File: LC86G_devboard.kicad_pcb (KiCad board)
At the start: 4 copper layers, 40 x 40 mm, 15 parts, among them J1 Conn_01x09_Pin, J2 U.FL-R-SMT_10_, Q1 DTC143Z, Q2 DTC143Z, Q3 AO3415, U1 LC86G

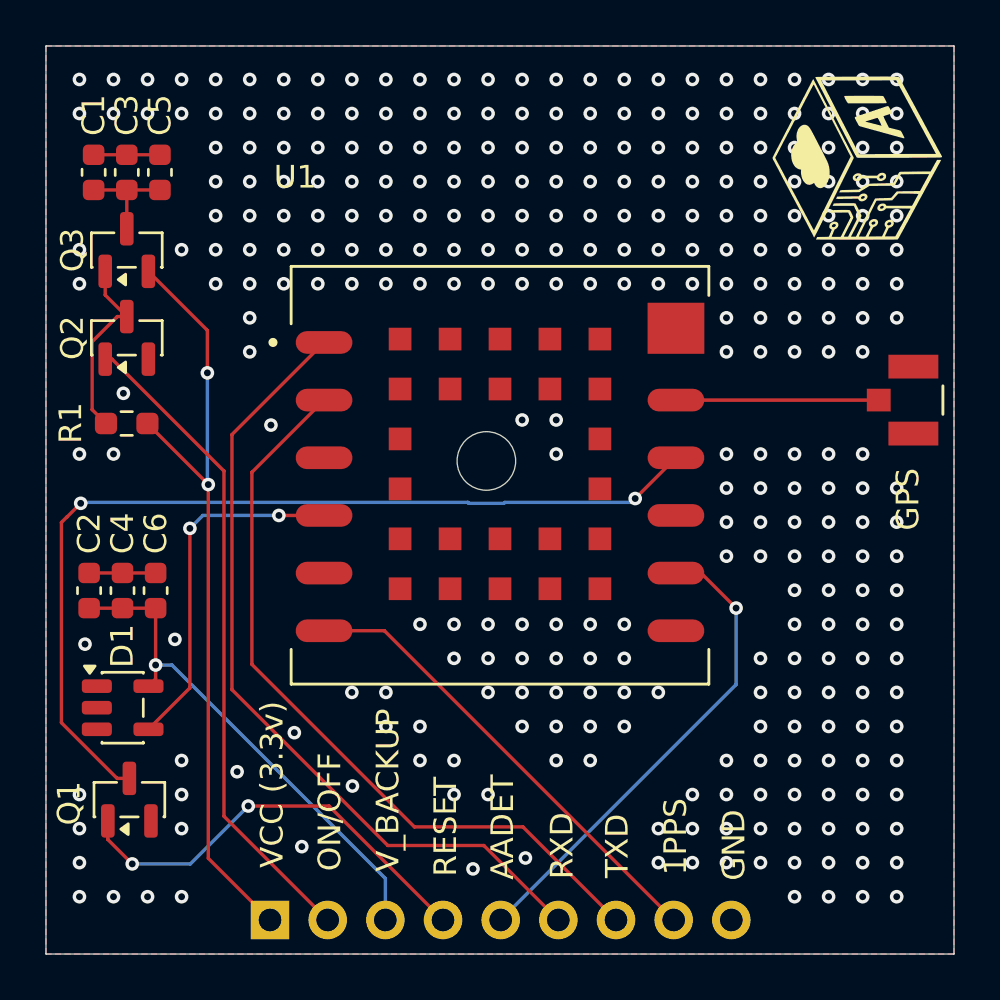
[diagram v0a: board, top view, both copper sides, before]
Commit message: pistas faltantes ruteadas
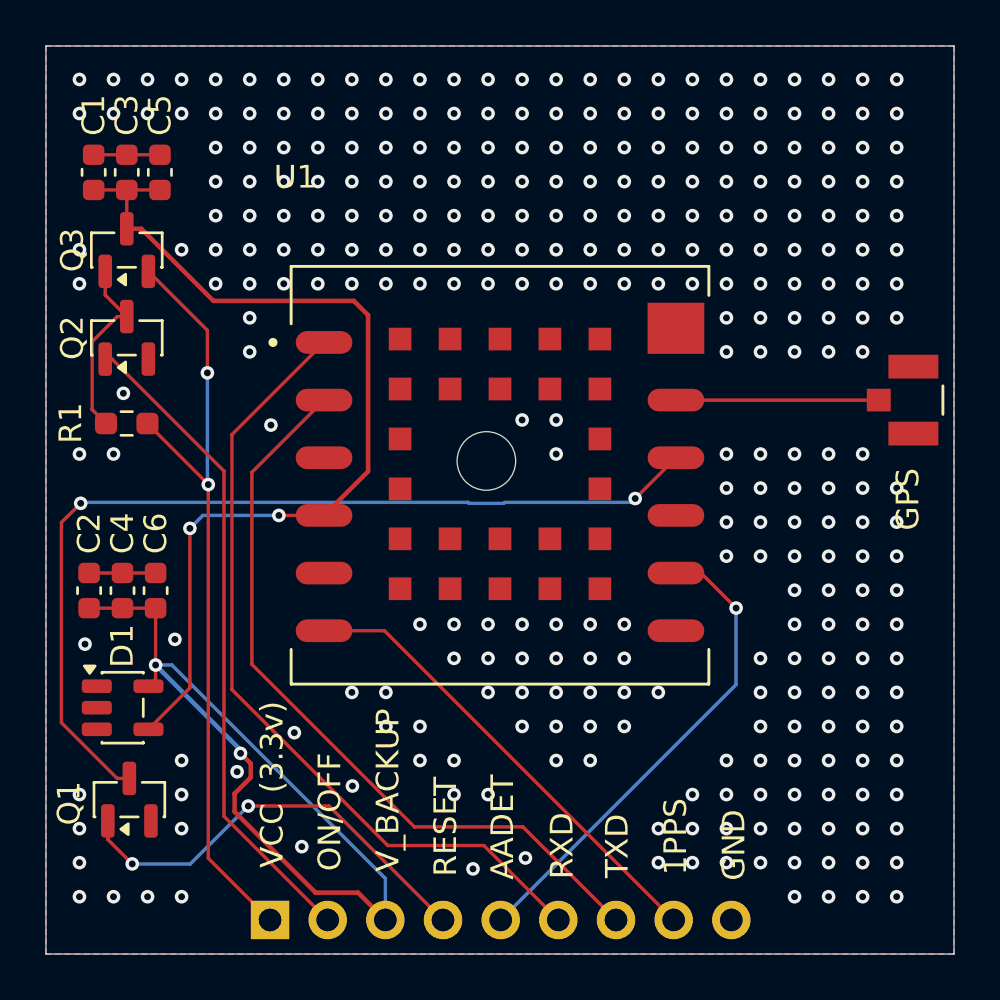
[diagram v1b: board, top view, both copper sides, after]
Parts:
- removed G***: LOGO, Images:LOGOv3.2
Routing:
- net /LC86G.VCC: track 20.5 -> 42.3 mm
- net /V_BCKP: track 22.4 -> 39.5 mm, vias 1 -> 2

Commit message: carga final
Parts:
- removed J1: Conn_01x09_Pin, Connector_PinHeader_2.54mm:PinHeader_1x09_P2.54mm_Vertical
- added D2: LED_Small, LED_SMD:LED_0603_1608Metric, F.Cu at (146.4, 106.2)
- added J3: Conn_01x10_Pin, Connector_PinHeader_2.54mm:PinHeader_1x10_P2.54mm_Vertical, B.Cu at (151.5, 109.1)
- added Power indicator: SolderJumper_2_Open, Jumper:SolderJumper-2_P1.3mm_Open_TrianglePad1.0x1.5mm, B.Cu at (145.2, 108.8)
- added R2: 4.7k, Resistor_SMD:R_0603_1608Metric_Pad0.98x0.95mm_HandSolder, F.Cu at (146.4, 108.6)
- added U2: XC6206P332MR, EasyEDA:SOT-23-3_L2.9-W1.6-P1.90-LS2.8-BR, F.Cu at (146.7, 102.9)
- added kibuzzard-6A1C8FBC: G***, kibuzzard-6A1C8FBC, F.Cu at (166.0, 73.1)
- moved Q1 4.67 mm to (146.7, 99.0), turned to 180 degrees
- moved D1 4.52 mm to (146.8, 95.2)
- moved C6 3.79 mm to (148.6, 90.8)
- moved C4 3.75 mm to (146.8, 90.8)
- moved C2 3.73 mm to (145.0, 90.8)
- moved C5 1.43 mm to (148.6, 74.7)
- moved C3 1.36 mm to (146.8, 74.7)
- moved C1 1.35 mm to (145.0, 74.7)
- moved R1 1.13 mm to (146.8, 86.0)
- moved Q3 0.97 mm to (146.8, 78.5)
- moved Q2 0.77 mm to (146.8, 82.6)
- moved J2 0.41 mm to (180.8, 86.1)
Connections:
- C2 pad 1: /V_BCKP -> /LC86G.V_BCKP
- C4 pad 1: /V_BCKP -> /LC86G.V_BCKP
- C6 pad 1: /V_BCKP -> /LC86G.V_BCKP
- D1 pad 5: /V_BCKP -> /LC86G.V_BCKP
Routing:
- net /V_BCKP: track 39.5 -> 0.00 mm, vias 2 -> 0
- net /LC86G.V_BCKP: track 0.00 -> 32.8 mm, vias 0 -> 2
- net /VCC: track 34.6 -> 45.6 mm, vias 2 -> 0
- net /LC86G.RESET: track 41.2 -> 32.0 mm, vias 2 -> 0
- net /LDO: track 0.00 -> 8.70 mm
- net /LC86G.VCC: track 42.3 -> 33.8 mm, vias 2 -> 0
- net Net-(JP1-A): track 0.00 -> 4.54 mm, vias 0 -> 1
- net GND: track 5.85 -> 9.54 mm, vias 308 -> 630
- net /LC86G.AADET: track 21.3 -> 18.1 mm, vias 1 -> 0
- net /ON/OFF: track 28.9 -> 31.7 mm, vias 0 -> 1
- net Net-(D2-K): track 0.00 -> 2.46 mm
- net /GPIO.RESET: track 19.2 -> 17.8 mm, vias 2 -> 0
- net /LC86G.1PPS: track 20.7 -> 21.8 mm, vias 0 -> 1
- net Net-(Q2-C): track 8.36 -> 7.31 mm
- net /LC86G.RXD: track 35.6 -> 36.4 mm, vias 0 -> 1
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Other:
- board text added: "+"
- board text added: "LDO"
- board text removed: "GND"

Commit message: aa
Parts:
- moved C1 7.00 mm to (151.7, 77.0)
- moved C3 6.82 mm to (153.2, 77.0)
- moved C5 6.62 mm to (154.8, 76.9)
- moved J2 4.85 mm to (176.1, 86.8)
- moved kibuzzard-6A1C8FBC 4.06 mm to (166.9, 77.1)
- moved U1 1.09 mm to (162.2, 90.1)
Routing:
- net GND: track 9.54 -> 14.4 mm, vias 630 -> 437
- net /LC86G.EX_ANT: track 8.52 -> 4.79 mm
- net /LC86G.RXD: track 36.4 -> 33.7 mm
- net /LC86G.TXD: track 32.9 -> 31.1 mm
- net /LC86G.RESET: track 32.0 -> 30.7 mm
- net /LC86G.AADET: track 18.1 -> 17.0 mm
- net /LC86G.1PPS: track 21.8 -> 22.4 mm
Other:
- board size 40 x 40 mm -> 35 x 35 mm
